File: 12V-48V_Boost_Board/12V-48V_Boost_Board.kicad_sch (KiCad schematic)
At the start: 3 parts

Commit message: Implemented feedback from request
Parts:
- added F2: 3A, Fuse:Fuse_0805_2012Metric_Pad1.15x1.40mm_HandSolder, symbol Device:Fuse
- added J1: 12V Input, TerminalBlock_Phoenix:TerminalBlock_Phoenix_PT-1,5-2-5.0-H_1x02_P5.00mm_Horizontal, symbol Connector:Screw_Terminal_01x02
- added J2: Input Current Sensing, TerminalBlock_Phoenix:TerminalBlock_Phoenix_PT-1,5-2-5.0-H_1x02_P5.00mm_Horizontal, symbol Connector:Screw_Terminal_01x02
- added J3: Output Current Sensing, TerminalBlock_Phoenix:TerminalBlock_Phoenix_PT-1,5-2-5.0-H_1x02_P5.00mm_Horizontal, symbol Connector:Screw_Terminal_01x02
- added J4: 48V Output, TerminalBlock_Phoenix:TerminalBlock_Phoenix_PT-1,5-2-5.0-H_1x02_P5.00mm_Horizontal, symbol Connector:Screw_Terminal_01x02
- added TH1: 20A, symbol Device:Thermistor_US
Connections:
- net Boost_Board_Chip/12V_INPUT: now also TH1.2; no longer F1.2
- net Boost_Board_Chip/48V_OUTPUT: now also F2.1; no longer R2.1
- net GND: now also J1.1 (Pin_1), J4.2 (Pin_2); no longer R2.2
- net at F1.1, R1.2: now also J2.2 (Pin_2)
- net +12V: no longer names the net of R1.1
- net +12V: now also J1.2 (Pin_2), J2.1 (Pin_1)
- new net: J3.2 (Pin_2), J4.1 (Pin_1), R2.2
- new net: F1.2, TH1.1
- new net: F2.2, J3.1 (Pin_1), R2.1
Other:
- moved on the sheet: F1, R1, R2

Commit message: Changed mosfet symbol to be more accurate to proposed mosfet
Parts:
- TH1: footprint (none) -> Library:Inrush Current Limiter
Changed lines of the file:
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@@
 			)
 		)
-		(property "Footprint" ""
+		(property "Footprint" "Library:Inrush Current Limiter"
 			(at 128.27 99.06 0)
 			(effects

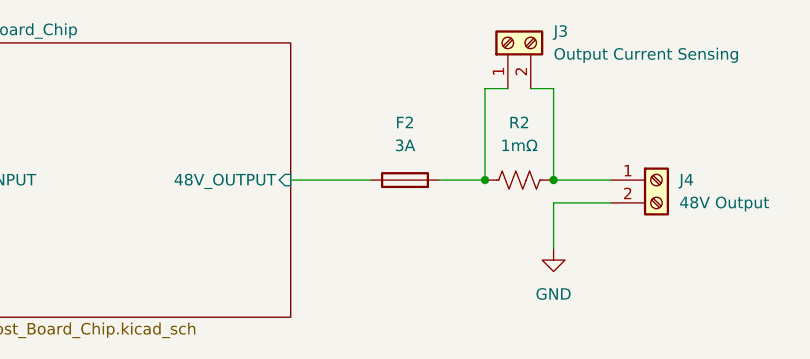
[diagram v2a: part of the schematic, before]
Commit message: Implemented feedback from request V2
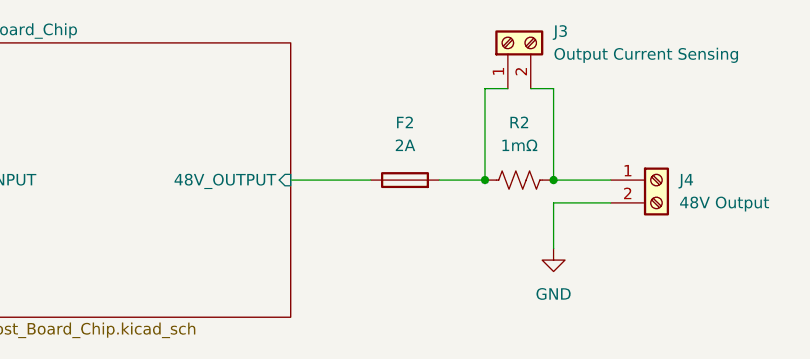
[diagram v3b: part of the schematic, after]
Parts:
- F1: footprint Fuse:Fuse_0805_2012Metric_Pad1.15x1.40mm_HandSolder -> Fuse:Fuse_1206_3216Metric
- F2: value 3A -> 2A; footprint Fuse:Fuse_0805_2012Metric_Pad1.15x1.40mm_HandSolder -> Fuse:Fuse_1206_3216Metric
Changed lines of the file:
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@@
 			)
 		)
-		(property "Footprint" "Fuse:Fuse_0805_2012Metric_Pad1.15x1.40mm_HandSolder"
+		(property "Footprint" "Fuse:Fuse_1206_3216Metric"
 			(at 115.57 100.838 90)
 			(effects
@@
 			)
 		)
-		(property "Datasheet" "~"
+		(property "Datasheet" "https://us.schurter.com/en/datasheet/typ_UST_1206.pdf"
 			(at 115.57 99.06 0)
 			(effects
@@
 			)
 		)
-		(property "Value" "3A"
+		(property "Value" "2A"
 			(at 190.5 95.25 90)
 			(effects
@@
 			)
 		)
-		(property "Footprint" "Fuse:Fuse_0805_2012Metric_Pad1.15x1.40mm_HandSolder"
+		(property "Footprint" "Fuse:Fuse_1206_3216Metric"
 			(at 190.5 100.838 90)
 			(effects
@@
 			)
 		)
-		(property "Datasheet" "~"
+		(property "Datasheet" "https://www.digikey.ca/en/products/detail/bel-fuse-inc/C1F-2/4968250"
 			(at 190.5 99.06 0)
 			(effects

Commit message: Implemented feedback from review V3
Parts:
- added DNP1: 1mΩ, Resistor_SMD:R_0805_2012Metric_Pad1.20x1.40mm_HandSolder, symbol Device:R_US
- added DNP2: ~, Resistor_SMD:R_0805_2012Metric_Pad1.20x1.40mm_HandSolder, symbol Device:R_US
- added J5: Output Measuring, TerminalBlock_Phoenix:TerminalBlock_Phoenix_PT-1,5-2-5.0-H_1x02_P5.00mm_Horizontal, symbol Connector:Screw_Terminal_01x02
- TH1: footprint Library:Inrush Current Limiter -> 12/48 boost:Inrush Current Limiter
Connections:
- net GND: now also DNP2.1, J5.2 (Pin_2); no longer J4.2 (Pin_2)
- new net: DNP1.1, DNP2.2, J5.1 (Pin_1)
- new net: DNP1.2, J4.2 (Pin_2)

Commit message: Made all the changes, still working on the refining the track sizes
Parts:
- R3: renamed from DNP1; value 1mΩ -> DNP
- R4: renamed from DNP2; value ~ -> DNP
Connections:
- net at J3.2 (Pin_2), J4.1 (Pin_1), R2.2: now also R3.2
- net at J4.2 (Pin_2): no longer R3.2
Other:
- moved on the sheet: J4, J5, R3, R4
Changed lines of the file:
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@@
 	)
 	(junction
-		(at 203.2 115.57)
+		(at 218.44 113.03)
+		(diameter 0)
+		(color 0 0 0 0)
+	)
+	(junction
+		(at 218.44 99.06)
 		(diameter 0)
 		(color 0 0 0 0)
@@
 	)
 	(junction
-		(at 203.2 123.19)
+		(at 218.44 120.65)
 		(diameter 0)
 		(color 0 0 0 0)
@@
 	(wire
 		(pts
-			(xy 218.44 120.65) (xy 218.44 123.19)
+			(xy 233.68 118.11) (xy 233.68 120.65)
 		)
 		(stroke
@@
 	(wire
 		(pts
-			(xy 218.44 118.11) (xy 218.44 115.57)
-		)
-		(stroke
-			(width 0)
-			(type default)
-		)
-	)
-	(wire
-		(pts
-			(xy 203.2 101.6) (xy 213.36 101.6)
+			(xy 233.68 115.57) (xy 233.68 113.03)
 		)
 		(stroke
@@
 	(wire
 		(pts
-			(xy 218.44 115.57) (xy 203.2 115.57)
+			(xy 233.68 113.03) (xy 218.44 113.03)
 		)
 		(stroke
@@
 	(wire
 		(pts
-			(xy 203.2 113.03) (xy 203.2 115.57)
+			(xy 218.44 110.49) (xy 218.44 113.03)
 		)
 		(stroke
@@
 	(wire
 		(pts
-			(xy 203.2 123.19) (xy 203.2 127)
-		)
-		(stroke
-			(width 0)
-			(type default)
-		)
-	)
-	(wire
-		(pts
-			(xy 203.2 101.6) (xy 203.2 105.41)
+			(xy 218.44 99.06) (xy 207.01 99.06)
+		)
+		(stroke
+			(width 0)
+			(type default)
+		)
+	)
+	(wire
+		(pts
+			(xy 218.44 120.65) (xy 218.44 127)
+		)
+		(stroke
+			(width 0)
+			(type default)
+		)
+	)
+	(wire
+		(pts
+			(xy 218.44 99.06) (xy 218.44 102.87)
 		)
 		(stroke
@@
 	(wire
 		(pts
-			(xy 213.36 99.06) (xy 207.01 99.06)
+			(xy 233.68 99.06) (xy 218.44 99.06)
 		)
 		(stroke
@@
 	(wire
 		(pts
-			(xy 218.44 123.19) (xy 203.2 123.19)
+			(xy 233.68 120.65) (xy 218.44 120.65)
 		)
 		(stroke
@@
 	(symbol
 		(lib_id "Connector:Screw_Terminal_01x02")
-		(at 223.52 118.11 0)
+		(at 238.76 115.57 0)
 		(unit 1)
 		(exclude_from_sim no)
@@
 		(fields_autoplaced yes)
 		(property "Reference" "J5"
-			(at 226.06 118.1099 0)
+			(at 241.3 115.5699 0)
 			(effects
 				(font
@@
 		)
 		(property "Value" "Output Measuring"
-			(at 226.06 120.6499 0)
+			(at 241.3 118.1099 0)
 			(effects
 				(font
@@
 		)
 		(property "Footprint" "TerminalBlock_Phoenix:TerminalBlock_Phoenix_PT-1,5-2-5.0-H_1x02_P5.00mm_Horizontal"
-			(at 223.52 118.11 0)
+			(at 238.76 115.57 0)
 			(effects
 				(font
@@
 		)
 		(property "Datasheet" "~"
-			(at 223.52 118.11 0)
+			(at 238.76 115.57 0)
 			(effects
 				(font
@@
 		)
 		(property "Description" "Generic screw terminal, single row, 01x02, script generated (kicad-library-utils/schlib/autogen/connector/)"
-			(at 223.52 118.11 0)
+			(at 238.76 115.57 0)
 			(effects
 				(font
@@
 	(symbol
 		(lib_id "Connector:Screw_Terminal_01x02")
-		(at 218.44 99.06 0)
+		(at 238.76 99.06 0)
 		(unit 1)
 		(exclude_from_sim no)
@@
 		(fields_autoplaced yes)
 		(property "Reference" "J4"
-			(at 220.98 99.0599 0)
+			(at 241.3 99.0599 0)
 			(effects
 				(font
@@
 		)
 		(property "Value" "48V Output"
-			(at 220.98 101.5999 0)
+			(at 241.3 101.5999 0)
 			(effects
 				(font
@@
 		)
 		(property "Footprint" "TerminalBlock_Phoenix:TerminalBlock_Phoenix_PT-1,5-2-5.0-H_1x02_P5.00mm_Horizontal"
-			(at 218.44 99.06 0)
+			(at 238.76 99.06 0)
 			(effects
 				(font
@@
 		)
 		(property "Datasheet" "~"
-			(at 218.44 99.06 0)
+			(at 238.76 99.06 0)
 			(effects
 				(font
@@
 		)
 		(property "Description" "Generic screw terminal, single row, 01x02, script generated (kicad-library-utils/schlib/autogen/connector/)"
-			(at 218.44 99.06 0)
+			(at 238.76 99.06 0)
 			(effects
 				(font
@@
 	(symbol
 		(lib_id "power:GND")
-		(at 203.2 127 0)
+		(at 218.44 127 0)
 		(unit 1)
 		(exclude_from_sim no)
@@
 		(fields_autoplaced yes)
 		(property "Reference" "#PWR02"
-			(at 203.2 133.35 0)
+			(at 218.44 133.35 0)
 			(effects
 				(font
@@
 		)
 		(property "Value" "GND"
-			(at 203.2 132.08 0)
+			(at 218.44 132.08 0)
 			(effects
 				(font
@@
 		)
 		(property "Footprint" ""
-			(at 203.2 127 0)
+			(at 218.44 127 0)
 			(effects
 				(font
@@
 		)
 		(property "Datasheet" ""
-			(at 203.2 127 0)
+			(at 218.44 127 0)
 			(effects
 				(font
@@
 		)
 		(property "Description" "Power symbol creates a global label with name \"GND\" , ground"
-			(at 203.2 127 0)
+			(at 218.44 127 0)
 			(effects
 				(font
@@
 	(symbol
 		(lib_id "Device:R_US")
-		(at 203.2 109.22 180)
+		(at 218.44 106.68 180)
 		(unit 1)
 		(exclude_from_sim no)
@@
 		(dnp no)
 		(fields_autoplaced yes)
-		(property "Reference" "DNP1"
-			(at 205.74 107.9499 0)
+		(property "Reference" "R3"
+			(at 220.98 105.4099 0)
 			(effects
 				(font
@@
 			)
 		)
-		(property "Value" "1mΩ"
-			(at 205.74 110.4899 0)
+		(property "Value" "DNP"
+			(at 220.98 107.9499 0)
 			(effects
 				(font
@@
 				)
 				(justify right)
-				(hide yes)
 			)
 		)
 		(property "Footprint" "Resistor_SMD:R_0805_2012Metric_Pad1.20x1.40mm_HandSolder"
-			(at 202.184 108.966 90)
+			(at 217.424 106.426 90)
 			(effects
 				(font
@@
 		)
 		(property "Datasheet" "~"
-			(at 203.2 109.22 0)
+			(at 218.44 106.68 0)
 			(effects
 				(font
@@
 		)
 		(property "Description" "Resistor, US symbol"
-			(at 203.2 109.22 0)
+			(at 218.44 106.68 0)
 			(effects
 				(font
@@
 			(project "12V-48V_Boost_Board"
 				(path "/3a220cd2-54b9-463d-ba95-4a8308a2a2d6"
-					(reference "DNP1")
+					(reference "R3")
 					(unit 1)
 				)
@@
 	(symbol
 		(lib_id "Device:R_US")
-		(at 203.2 119.38 180)
+		(at 218.44 116.84 180)
 		(unit 1)
 		(exclude_from_sim no)
@@
 		(dnp no)
 		(fields_autoplaced yes)
-		(property "Reference" "DNP2"
-			(at 205.74 118.1099 0)
+		(property "Reference" "R4"
+			(at 220.98 115.5699 0)
 			(effects
 				(font
@@
 			)
 		)
-		(property "Value" "~"
-			(at 205.74 120.6499 0)
+		(property "Value" "DNP"
+			(at 220.98 118.1099 0)
 			(effects
 				(font
@@
 		)
 		(property "Footprint" "Resistor_SMD:R_0805_2012Metric_Pad1.20x1.40mm_HandSolder"
-			(at 202.184 119.126 90)
+			(at 217.424 116.586 90)
 			(effects
 				(font
@@
 		)
 		(property "Datasheet" "~"
-			(at 203.2 119.38 0)
+			(at 218.44 116.84 0)
 			(effects
 				(font
@@
 		)
 		(property "Description" "Resistor, US symbol"
-			(at 203.2 119.38 0)
+			(at 218.44 116.84 0)
 			(effects
 				(font
@@
 			(project "12V-48V_Boost_Board"
 				(path "/3a220cd2-54b9-463d-ba95-4a8308a2a2d6"
-					(reference "DNP2")
-					(unit 1)
-				)
+					(reference "R4")
+					(unit 1)
+				)

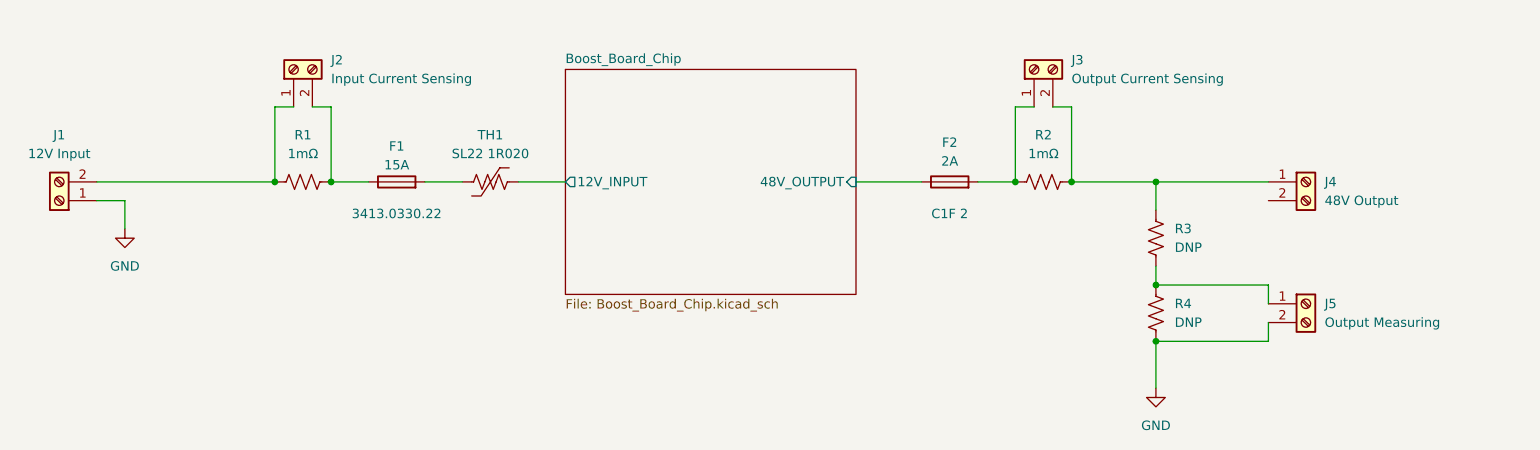
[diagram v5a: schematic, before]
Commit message: Made some changes to track sizes
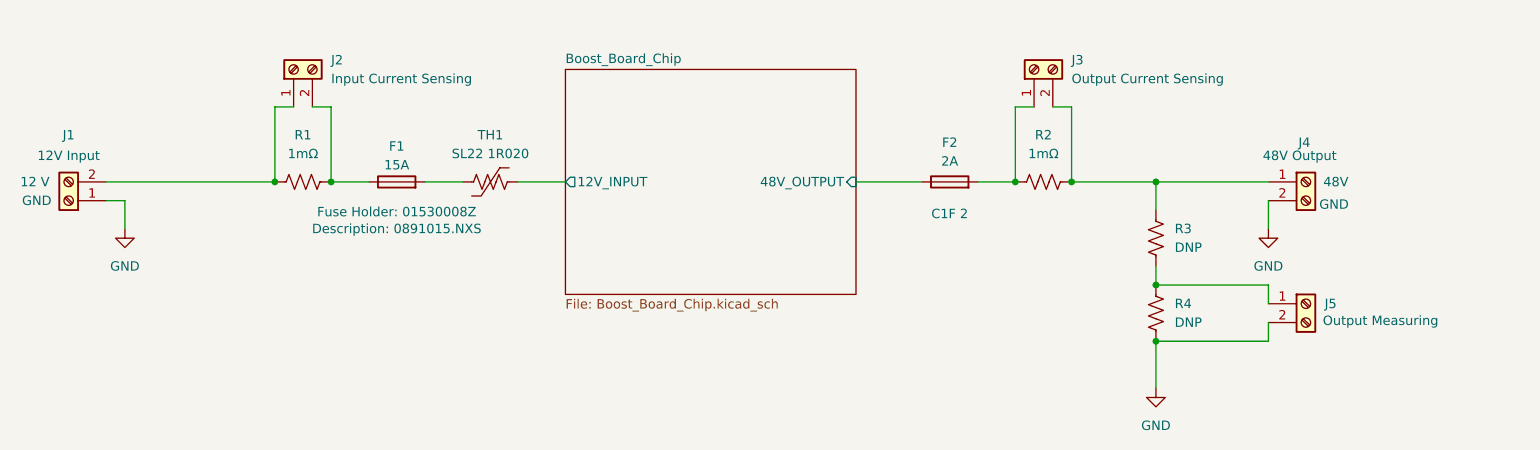
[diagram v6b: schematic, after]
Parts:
- F1: footprint Fuse:Fuse_1206_3216Metric -> 12/48 boost:01530009Z; Fuse Holder (none) -> 01530008Z
- J1: Input 1 (none) -> GND; Input 2 (none) -> 12 V
- J4: Output 1 (none) -> GND; Output 2 (none) -> 48V
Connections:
- net GND: now also J4.2 (Pin_2)
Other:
- moved on the sheet: J1
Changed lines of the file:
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@@
 	(wire
 		(pts
-			(xy 74.93 99.06) (xy 99.06 99.06)
+			(xy 76.2 99.06) (xy 99.06 99.06)
 		)
 		(stroke
@@
 	(wire
 		(pts
+			(xy 233.68 101.6) (xy 233.68 105.41)
+		)
+		(stroke
+			(width 0)
+			(type default)
+		)
+	)
+	(wire
+		(pts
 			(xy 218.44 120.65) (xy 218.44 127)
 		)
@@
 	(wire
 		(pts
-			(xy 74.93 101.6) (xy 78.74 101.6)
+			(xy 76.2 101.6) (xy 78.74 101.6)
 		)
 		(stroke
@@
 		(on_board yes)
 		(dnp no)
-		(fields_autoplaced yes)
 		(property "Reference" "J5"
 			(at 241.3 115.5699 0)
@@
 		)
 		(property "Value" "Output Measuring"
-			(at 241.3 118.1099 0)
+			(at 241.046 117.856 0)
 			(effects
 				(font
@@
 		(on_board yes)
 		(dnp no)
-		(fields_autoplaced yes)
 		(property "Reference" "J4"
-			(at 241.3 99.0599 0)
+			(at 237.744 93.726 0)
 			(effects
 				(font
@@
 		)
 		(property "Value" "48V Output"
-			(at 241.3 101.5999 0)
+			(at 232.918 95.504 0)
 			(effects
 				(font
@@
 				)
 				(hide yes)
+			)
+		)
+		(property "Output 1" "GND"
+			(at 242.57 102.108 0)
+			(effects
+				(font
+					(size 1.27 1.27)
+				)
+			)
+		)
+		(property "Output 2" "48V"
+			(at 242.824 99.06 0)
+			(effects
+				(font
+					(size 1.27 1.27)
+				)
 			)
 		)
@@
 			)
 		)
-		(property "Footprint" "Fuse:Fuse_1206_3216Metric"
+		(property "Footprint" "12/48 boost:01530009Z"
 			(at 115.57 100.838 90)
 			(effects
@@
 			)
 		)
-		(property "Datasheet" "https://us.schurter.com/en/datasheet/typ_UST_1206.pdf"
+		(property "Datasheet" "https://www.littelfuse.com/assetdocs/littelfuse-datasheet-891-lp-mini?assetguid=748f2a1b-6fd1-43cb-b900-7178f45585a0"
 			(at 115.57 99.06 0)
 			(effects
@@
 			)
 		)
-		(property "Description" "3413.0330.22"
-			(at 115.57 103.378 90)
+		(property "Description" "0891015.NXS"
+			(at 115.57 105.41 90)
+			(show_name yes)
+			(effects
+				(font
+					(size 1.27 1.27)
+				)
+			)
+		)
+		(property "Fuse Holder" "01530008Z"
+			(at 115.57 103.124 90)
+			(show_name yes)
 			(effects
 				(font
@@
 				(path "/3a220cd2-54b9-463d-ba95-4a8308a2a2d6"
 					(reference "F1")
+					(unit 1)
+				)
+			)
+		)
+	)
+	(symbol
+		(lib_id "power:GND")
+		(at 233.68 105.41 0)
+		(unit 1)
+		(exclude_from_sim no)
+		(in_bom yes)
+		(on_board yes)
+		(dnp no)
+		(fields_autoplaced yes)
+		(property "Reference" "#PWR016"
+			(at 233.68 111.76 0)
+			(effects
+				(font
+					(size 1.27 1.27)
+				)
+				(hide yes)
+			)
+		)
+		(property "Value" "GND"
+			(at 233.68 110.49 0)
+			(effects
+				(font
+					(size 1.27 1.27)
+				)
+			)
+		)
+		(property "Footprint" ""
+			(at 233.68 105.41 0)
+			(effects
+				(font
+					(size 1.27 1.27)
+				)
+				(hide yes)
+			)
+		)
+		(property "Datasheet" ""
+			(at 233.68 105.41 0)
+			(effects
+				(font
+					(size 1.27 1.27)
+				)
+				(hide yes)
+			)
+		)
+		(property "Description" "Power symbol creates a global label with name \"GND\" , ground"
+			(at 233.68 105.41 0)
+			(effects
+				(font
+					(size 1.27 1.27)
+				)
+				(hide yes)
+			)
+		)
+		(pin "1"
+		)
+		(instances
+			(project "12V-48V_Boost_Board"
+				(path "/3a220cd2-54b9-463d-ba95-4a8308a2a2d6"
+					(reference "#PWR016")
 					(unit 1)
 				)
@@
 	(symbol
 		(lib_id "Connector:Screw_Terminal_01x02")
-		(at 69.85 101.6 180)
+		(at 71.12 101.6 180)
 		(unit 1)
 		(exclude_from_sim no)
@@
 		(on_board yes)
 		(dnp no)
-		(fields_autoplaced yes)
 		(property "Reference" "J1"
-			(at 69.85 92.71 0)
+			(at 71.12 92.71 0)
 			(effects
 				(font
@@
 		)
 		(property "Value" "12V Input"
-			(at 69.85 95.25 0)
+			(at 71.12 95.504 0)
 			(effects
 				(font
@@
 		)
 		(property "Footprint" "TerminalBlock_Phoenix:TerminalBlock_Phoenix_PT-1,5-2-5.0-H_1x02_P5.00mm_Horizontal"
-			(at 69.85 101.6 0)
+			(at 71.12 101.6 0)
 			(effects
 				(font
@@
 		)
 		(property "Datasheet" "~"
-			(at 69.85 101.6 0)
+			(at 71.12 101.6 0)
 			(effects
 				(font
@@
 		)
 		(property "Description" "Generic screw terminal, single row, 01x02, script generated (kicad-library-utils/schlib/autogen/connector/)"
-			(at 69.85 101.6 0)
-			(effects
-				(font
-					(size 1.27 1.27)
-				)
-				(hide yes)
-			)
-		)
+			(at 71.12 101.6 0)
+			(effects
+				(font
+					(size 1.27 1.27)
+				)
+				(hide yes)
+			)
+		)
+		(property "Input 1" "GND"
+			(at 66.802 101.6 0)
+			(effects
+				(font
+					(size 1.27 1.27)
+				)
+			)
+		)
+		(property "Input 2" "12 V"
+			(at 66.548 99.06 0)
+			(effects
+				(font
+					(size 1.27 1.27)
+				)
+			)
+		)

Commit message: Made some schematic and labelling changes, going to probably revamp the entire layout cause I'm pretty unhappy with it and now see the recommended one from the datasheet
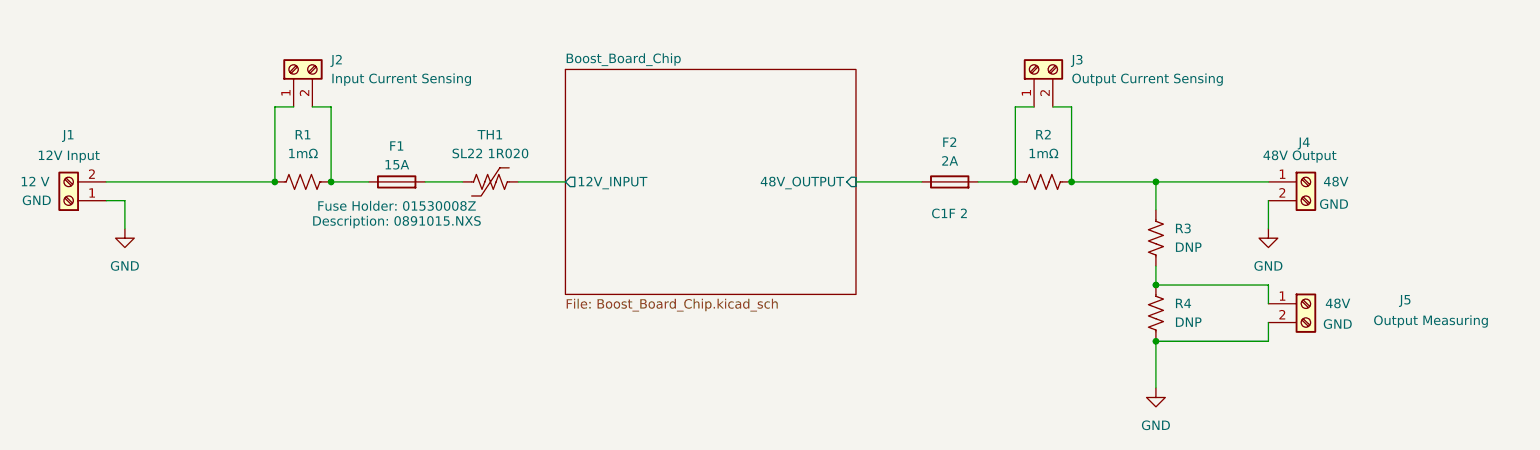
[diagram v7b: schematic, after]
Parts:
- J5: Output 1 (none) -> 48V; Output 2 (none) -> GND
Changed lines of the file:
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@@
 		(dnp no)
 		(property "Reference" "J5"
-			(at 241.3 115.5699 0)
+			(at 251.46 115.062 0)
 			(effects
 				(font
@@
 		)
 		(property "Value" "Output Measuring"
-			(at 241.046 117.856 0)
+			(at 247.904 117.856 0)
 			(effects
 				(font
@@
 				)
 				(hide yes)
+			)
+		)
+		(property "Output 1" "48V"
+			(at 243.078 115.57 0)
+			(effects
+				(font
+					(size 1.27 1.27)
+				)
+			)
+		)
+		(property "Output 2" "GND"
+			(at 243.078 118.364 0)
+			(effects
+				(font
+					(size 1.27 1.27)
+				)
 			)
 		)
@@
 		)
 		(property "Description" "0891015.NXS"
-			(at 115.57 105.41 90)
+			(at 115.57 104.394 90)
 			(show_name yes)
 			(effects
@@
 		)
 		(property "Fuse Holder" "01530008Z"
-			(at 115.57 103.124 90)
+			(at 115.57 102.362 90)
 			(show_name yes)
 			(effects
